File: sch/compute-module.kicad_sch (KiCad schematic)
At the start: 10 parts, among them J2 SAM10346-ND, J3 Conn_02x20_Odd_Even, M1 ComputeModule5-CM5, SW1 1825910-6

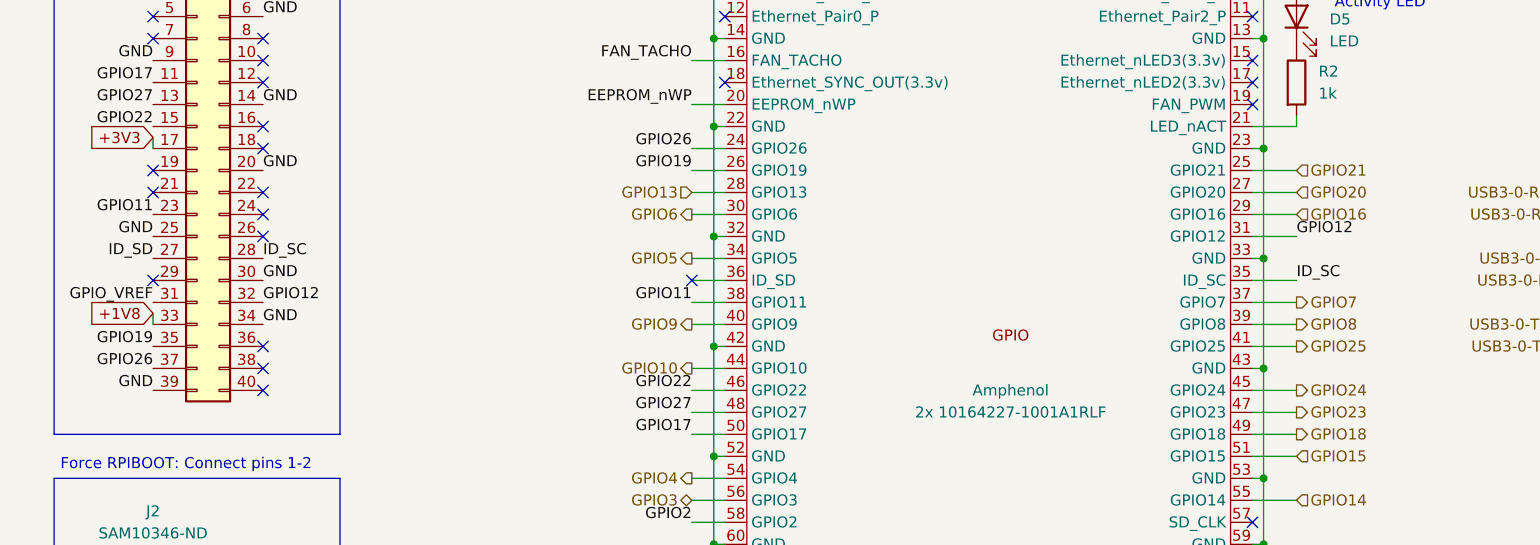
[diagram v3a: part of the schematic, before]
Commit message: partially route the powerlines
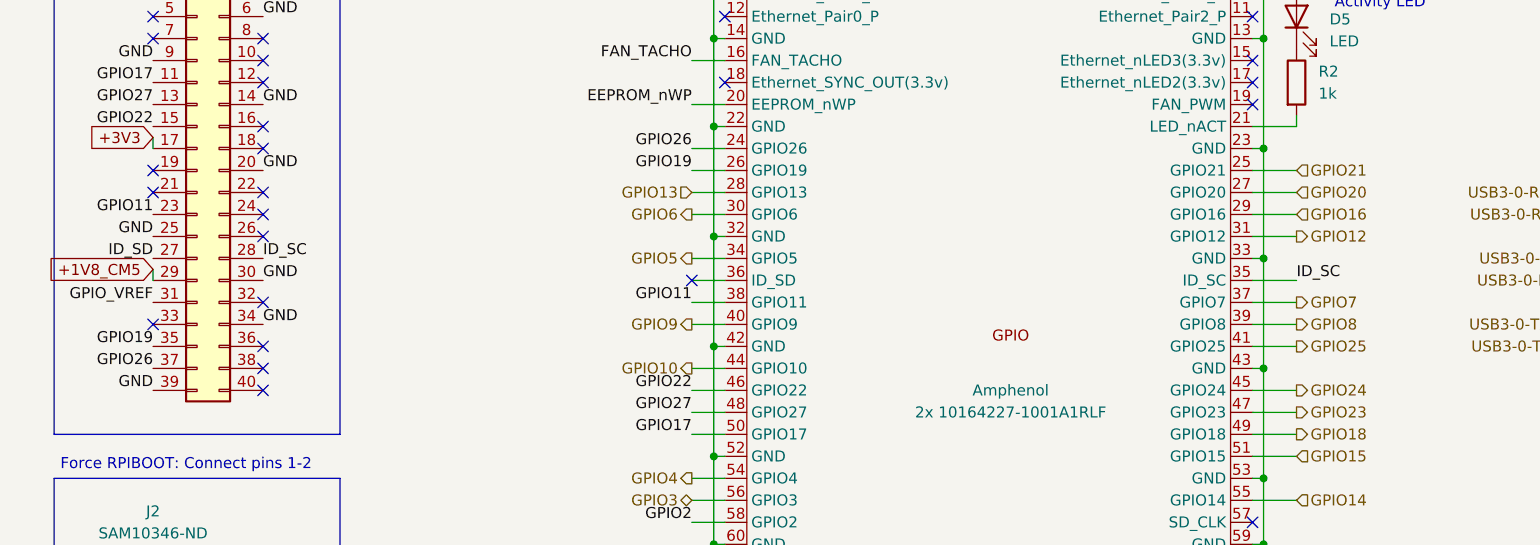
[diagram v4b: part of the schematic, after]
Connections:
- net +1V8_CM5: now also J3.29 (Pin_29)
- net GPIO12: no longer J3.32 (Pin_32)
- net +1V8: no longer names the net of J3.33 (Pin_33)
- no-connect marks 102 -> 103
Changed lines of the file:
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@@
+	)
+	(no_connect
+		(at 31.75 73.66)
 	)
 	(no_connect
@@
 	)
 	(no_connect
+		(at 44.45 71.12)
+	)
+	(no_connect
 		(at 201.93 35.56)
 	)
@@
 	)
 	(no_connect
-		(at 31.75 68.58)
-	)
-	(no_connect
 		(at 44.45 81.28)
 	)
@@
 	(wire
 		(pts
+			(xy 31.75 67.31) (xy 31.75 68.58)
+		)
+		(stroke
+			(width 0)
+			(type default)
+		)
+	)
+	(wire
+		(pts
 			(xy 262.89 38.1) (xy 266.7 38.1)
 		)
@@
 		(pts
 			(xy 80.01 134.62) (xy 93.98 134.62)
-		)
-		(stroke
-			(width 0)
-			(type default)
-		)
-	)
-	(wire
-		(pts
-			(xy 31.75 72.39) (xy 31.75 73.66)
 		)
 		(stroke
@@
 		)
 	)
-	(label "GPIO12"
-		(at 163.83 63.5 0)
-		(effects
-			(font
-				(size 1.27 1.27)
-			)
-			(justify left bottom)
-		)
-	)
 	(label "nRPIBOOT"
 		(at 161.29 142.24 0)
@@
 			)
 			(justify right bottom)
-		)
-	)
-	(label "GPIO12"
-		(at 44.45 71.12 0)
-		(effects
-			(font
-				(size 1.27 1.27)
-			)
-			(justify left bottom)
 		)
 	)
@@
 		)
 	)
-	(global_label "+1V8"
+	(global_label "+1V8_CM5"
 		(shape input)
-		(at 31.75 72.39 180)
+		(at 31.75 67.31 180)
 		(fields_autoplaced yes)
 		(effects
@@
 		)
 		(property "Intersheetrefs" "${INTERSHEET_REFS}"
-			(at 23.6848 72.39 0)
+			(at 23.6848 67.31 0)
 			(effects
 				(font
@@
 		)
 	)
+	(hierarchical_label "GPIO12"
+		(shape output)
+		(at 163.83 63.5 0)
+		(effects
+			(font
+				(size 1.27 1.27)
+			)
+			(justify left)
+		)
+	)

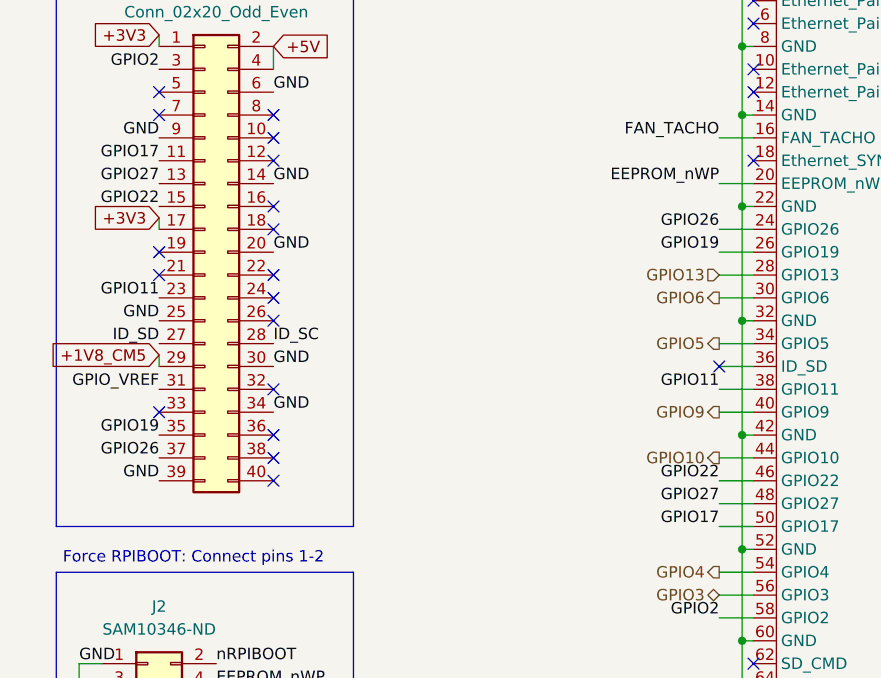
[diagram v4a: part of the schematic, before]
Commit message: powergrid complete, still missing antennas
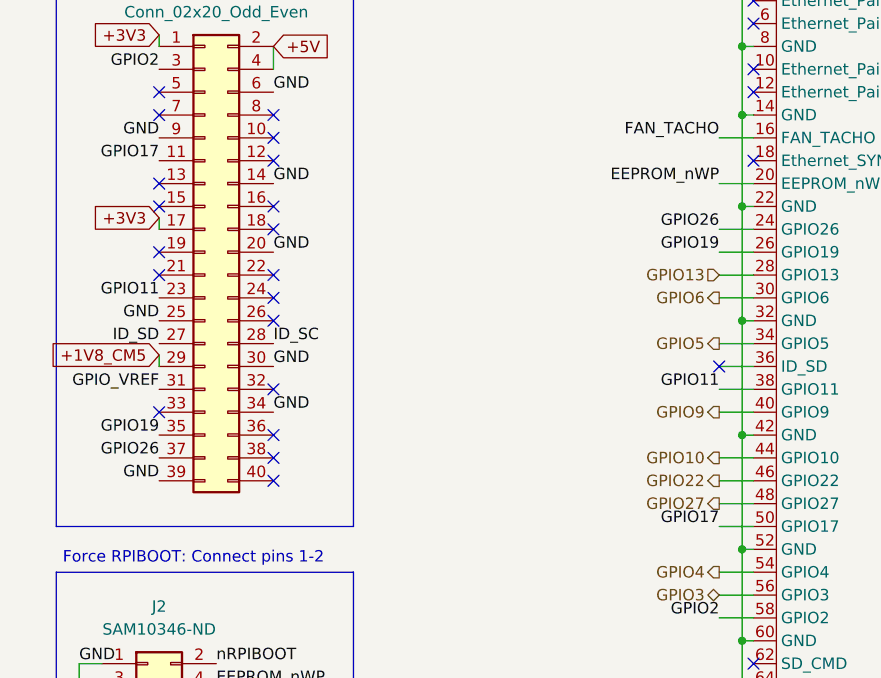
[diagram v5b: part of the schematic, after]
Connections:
- net GPIO22: no longer J3.15 (Pin_15)
- net GPIO27: no longer J3.13 (Pin_13)
- no-connect marks 103 -> 105
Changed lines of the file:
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@@
+	)
+	(no_connect
+		(at 31.75 50.8)
 	)
 	(no_connect
@@
 	(no_connect
 		(at 201.93 137.16)
+	)
+	(no_connect
+		(at 31.75 48.26)
 	)
 	(no_connect
@@
 		)
 	)
-	(label "GPIO22"
-		(at 93.98 81.28 180)
-		(effects
-			(font
-				(size 1.27 1.27)
-			)
-			(justify right bottom)
-		)
-	)
 	(label "GPIO2"
 		(at 93.98 96.52 180)
@@
 		)
 	)
-	(label "GPIO27"
-		(at 31.75 48.26 180)
-		(effects
-			(font
-				(size 1.27 1.27)
-			)
-			(justify right bottom)
-		)
-	)
 	(label "GND"
 		(at 44.45 38.1 0)
@@
 		)
 	)
-	(label "GPIO27"
-		(at 93.98 83.82 180)
-		(effects
-			(font
-				(size 1.27 1.27)
-			)
-			(justify right bottom)
-		)
-	)
 	(label "GPIO17"
 		(at 31.75 45.72 180)
-		(effects
-			(font
-				(size 1.27 1.27)
-			)
-			(justify right bottom)
-		)
-	)
-	(label "GPIO22"
-		(at 31.75 50.8 180)
 		(effects
 			(font
@@
 		)
 	)
+	(hierarchical_label "GPIO27"
+		(shape output)
+		(at 93.98 83.82 180)
+		(effects
+			(font
+				(size 1.27 1.27)
+			)
+			(justify right)
+		)
+	)
 	(hierarchical_label "USB3-0-TX_P"
 		(shape output)
@@
 		)
 	)
+	(hierarchical_label "GPIO22"
+		(shape output)
+		(at 93.98 81.28 180)
+		(effects
+			(font
+				(size 1.27 1.27)
+			)
+			(justify right)
+		)
+	)

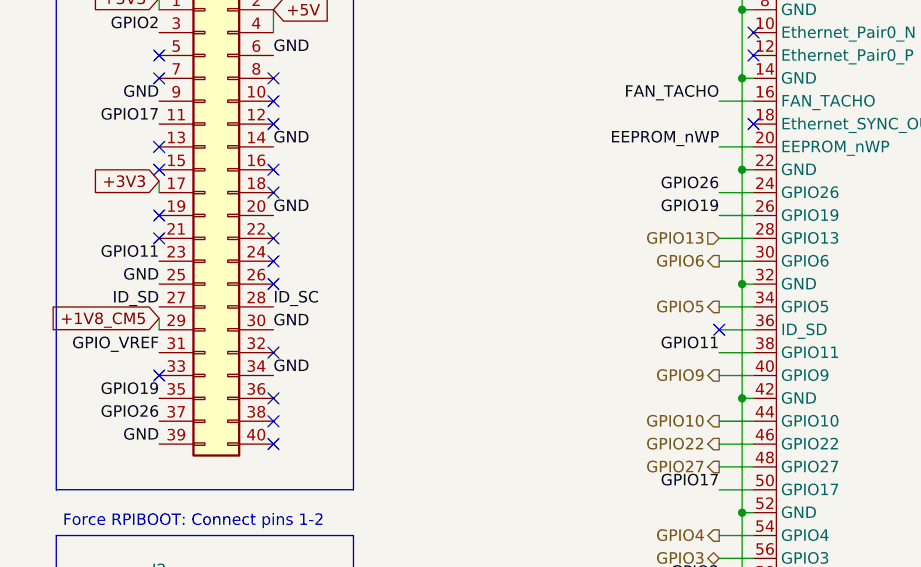
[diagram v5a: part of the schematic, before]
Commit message: solved more rule-conflicts, only rules left to solve is antenna traces, edgeplaced devices and grounding in simcard
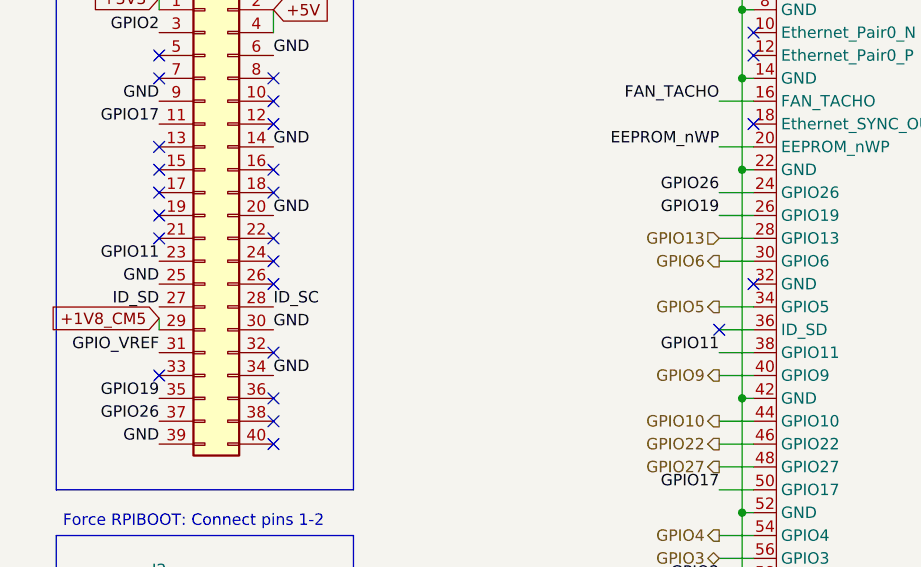
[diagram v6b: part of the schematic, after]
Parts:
- M1: footprint CM5108032:MODULE_CM5108032 -> CM5108032:Raspberry-Pi-5-Compute-Module
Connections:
- net +3V3: no longer J3.17 (Pin_17)
- net GND: no longer M1.32 (GND)
- no-connect marks 105 -> 107
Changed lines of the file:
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@@
 	)
 	(junction
-		(at 96.52 63.5)
-		(diameter 0)
-		(color 0 0 0 0)
-	)
-	(junction
 		(at 160.02 40.64)
 		(diameter 0)
@@
 	)
 	(no_connect
+		(at 31.75 53.34)
+	)
+	(no_connect
 		(at 201.93 137.16)
 	)
@@
 	)
 	(no_connect
+		(at 97.79 63.5)
+	)
+	(no_connect
 		(at 93.98 127)
 	)
@@
 	(wire
 		(pts
-			(xy 96.52 50.8) (xy 96.52 63.5)
+			(xy 96.52 50.8) (xy 96.52 76.2)
 		)
 		(stroke
@@
 	(wire
 		(pts
-			(xy 96.52 63.5) (xy 97.79 63.5)
-		)
-		(stroke
-			(width 0)
-			(type default)
-		)
-	)
-	(wire
-		(pts
 			(xy 158.75 106.68) (xy 160.02 106.68)
 		)
@@
 	(wire
 		(pts
-			(xy 31.75 52.07) (xy 31.75 53.34)
-		)
-		(stroke
-			(width 0)
-			(type default)
-		)
-	)
-	(wire
-		(pts
 			(xy 265.43 109.22) (xy 265.43 116.84)
 		)
@@
 	(wire
 		(pts
-			(xy 96.52 63.5) (xy 96.52 76.2)
-		)
-		(stroke
-			(width 0)
-			(type default)
-		)
-	)
-	(wire
-		(pts
 			(xy 199.39 63.5) (xy 201.93 63.5)
 		)
@@
 		)
 	)
-	(global_label "+3V3"
-		(shape input)
-		(at 31.75 52.07 180)
-		(fields_autoplaced yes)
-		(effects
-			(font
-				(size 1.27 1.27)
-			)
-			(justify right)
-		)
-		(property "Intersheetrefs" "${INTERSHEET_REFS}"
-			(at 23.6848 52.07 0)
-			(effects
-				(font
-					(size 1.27 1.27)
-				)
-				(justify right)
-				(hide yes)
-			)
-		)
-	)
 	(global_label "+1V8_CM5"
 		(shape output)
@@
 			)
 		)
-		(property "Footprint" "CM5108032:MODULE_CM5108032"
+		(property "Footprint" "CM5108032:Raspberry-Pi-5-Compute-Module"
 			(at 273.05 107.95 0)
 			(effects
@@
 			)
 		)
-		(property "Footprint" "CM5108032:MODULE_CM5108032"
+		(property "Footprint" "CM5108032:Raspberry-Pi-5-Compute-Module"
 			(at 234.95 113.03 0)
 			(effects

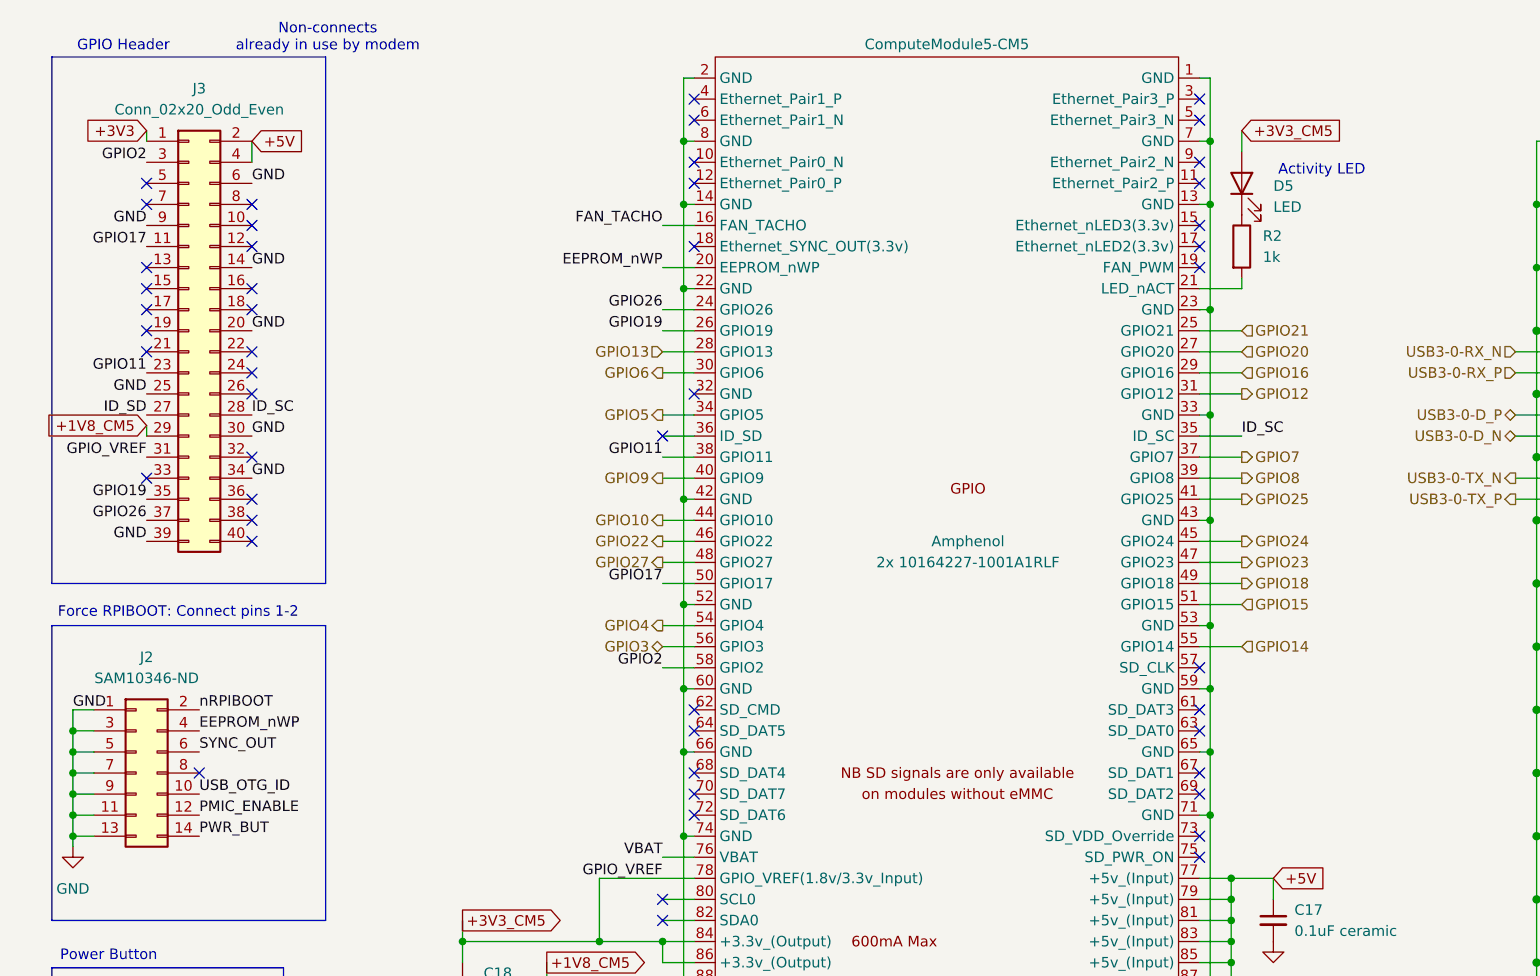
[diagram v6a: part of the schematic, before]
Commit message: fix incorrect gpio wiring and cleanup nets
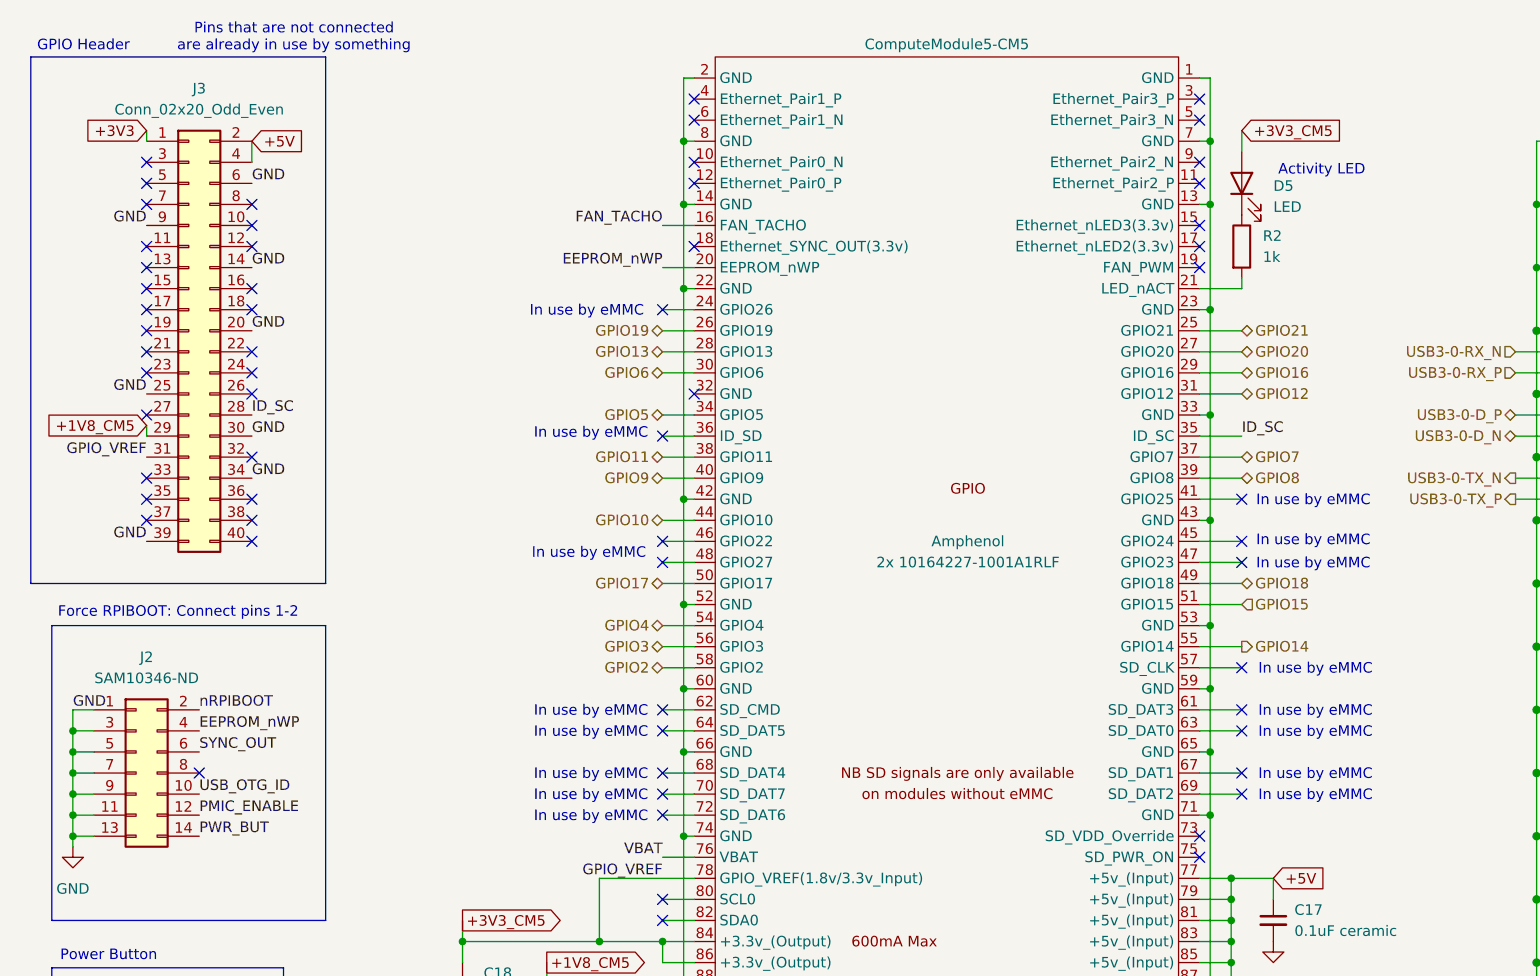
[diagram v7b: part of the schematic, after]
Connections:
- net GPIO11: no longer J3.23 (Pin_23)
- net GPIO17: no longer J3.11 (Pin_11)
- net GPIO19: no longer J3.35 (Pin_35)
- net GPIO2: no longer J3.3 (Pin_3)
- net GPIO22: no longer names the net of M1.46 (GPIO22)
- net GPIO23: no longer names the net of M1.47 (GPIO23)
- net GPIO24: no longer names the net of M1.45 (GPIO24)
- net GPIO25: no longer names the net of M1.41 (GPIO25)
- net GPIO26: no longer names the net of M1.24 (GPIO26)
- net GPIO26: no longer J3.37 (Pin_37)
- net GPIO27: no longer names the net of M1.48 (GPIO27)
- net ID_SD: no longer names the net of J3.27 (Pin_27)
- no-connect marks 107 -> 119
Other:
- note added: "In use by eMMC"
- note added: "Pins that are not connected are already in use by something"
- note removed: "Non-connects already in use by modem"
